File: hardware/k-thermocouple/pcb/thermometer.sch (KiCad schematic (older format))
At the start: 25 parts

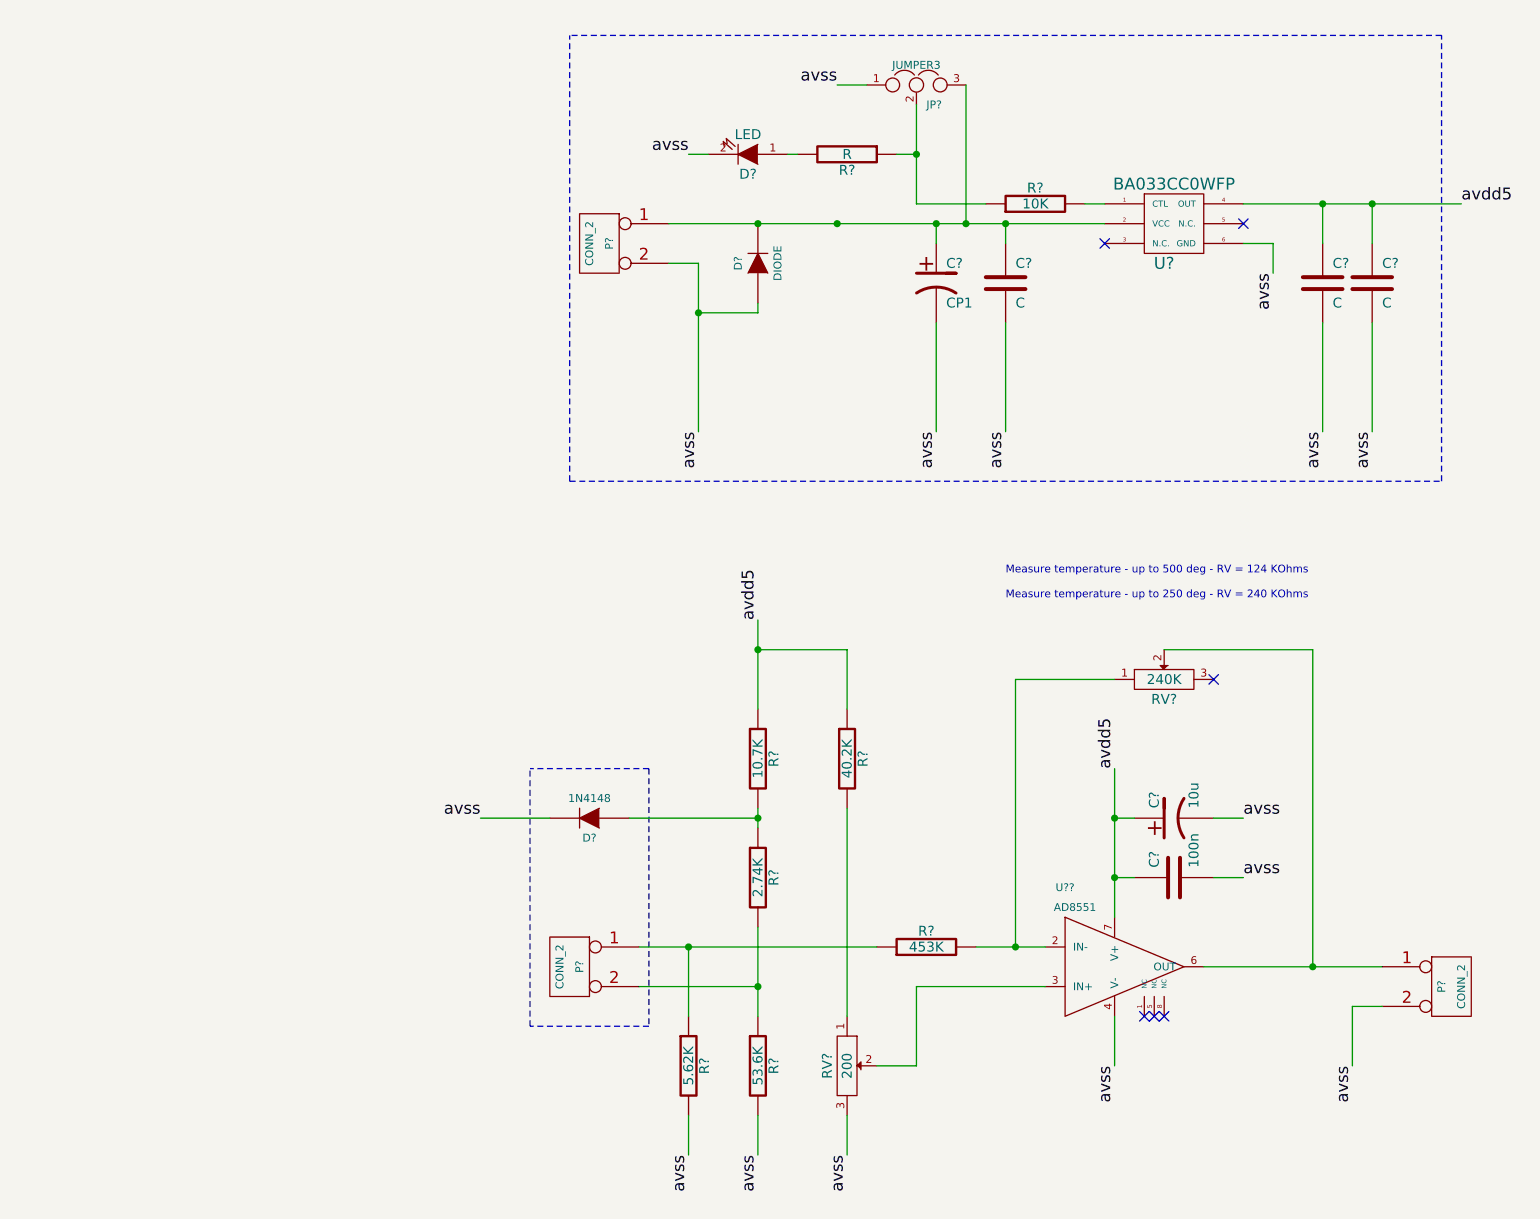
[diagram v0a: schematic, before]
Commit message: Schematic with AD8551 done and initial board started.
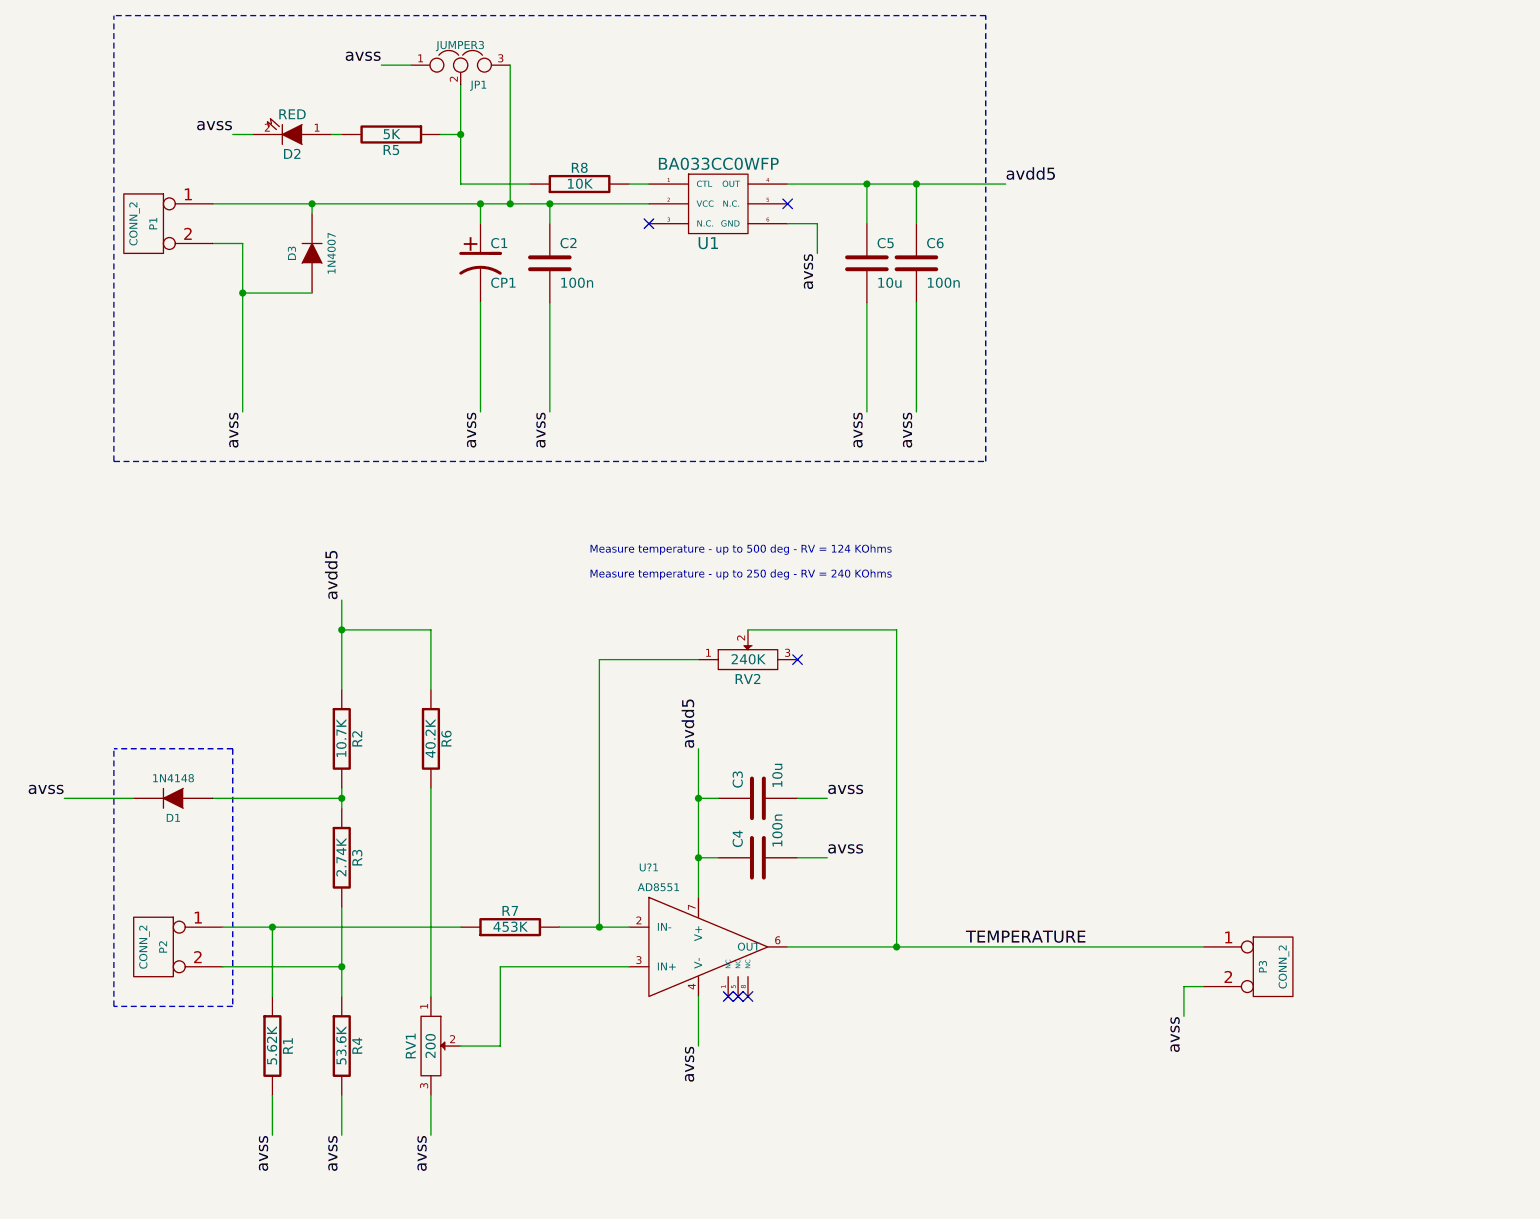
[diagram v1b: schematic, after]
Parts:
- removed C?: 10u, symbol CP1
- removed P?: CONN_2, symbol CONN_2
- added C3: 10u, SM0805, symbol C
- added P3: CONN_2, TS-501, symbol CONN_2
- C1: renamed from C?; footprint (none) -> CAP_POL_10u
- C2, C6: renamed from C?; value C -> 100n; footprint (none) -> SM0805
- C4: renamed from C?; footprint (none) -> SM0805
- C5: renamed from C?; value C -> 10u; footprint (none) -> SM0805
- D1: renamed from D?; footprint (none) -> melf
- D2: renamed from D?; value LED -> RED; footprint (none) -> KP-2012ZGC
- D3: renamed from D?; value DIODE -> 1N4007; footprint (none) -> melf
- JP1: renamed from JP?; footprint (none) -> JUMPER3
- P1: renamed from P?; footprint (none) -> TS-501
- P2: renamed from P?; footprint (none) -> 2EDGR
- R1, R2, R3, R4, R6, R7, R8: renamed from R?; footprint (none) -> SM0805
- R5: renamed from R?; value R -> 5K; footprint (none) -> SM0805
- RV1, RV2: renamed from RV?; footprint (none) -> BOURNS_TRIMMER
- U1: renamed from U?; footprint (none) -> BA033CCOWFP
- U?1: renamed from U??; footprint (none) -> MSOP_8
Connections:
- net avdd5: now also C3.1
- net avss: now also C3.2, P3.2 (PM)
- net TEMPERATURE: now reaches RV2.2, U?1.6 (OUT)
- net TEMPERATURE: now also P3.1 (P1)
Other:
- moved on the sheet: C1, C2, C4, C5, C6, D1, D2, D3, JP1, P1, P2, R1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

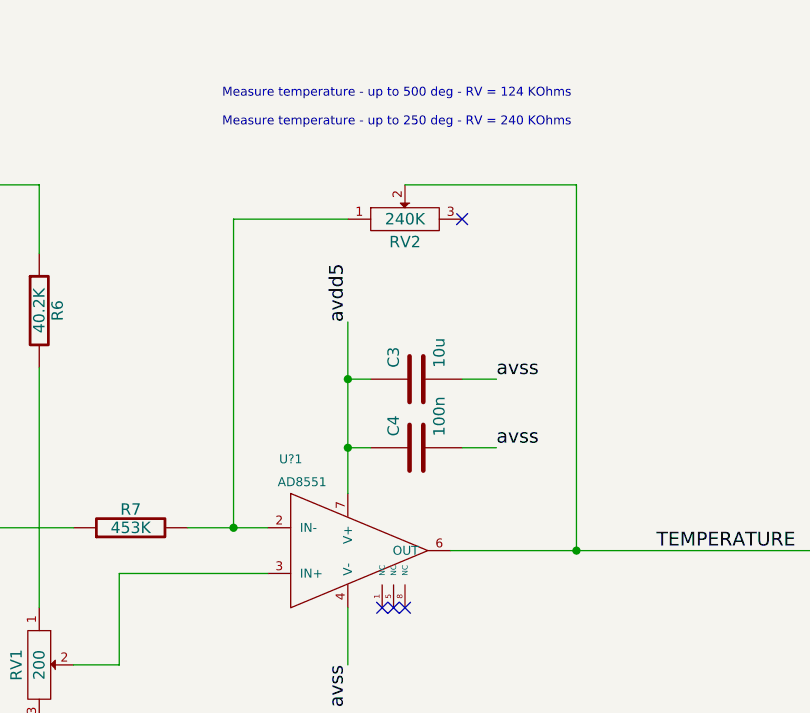
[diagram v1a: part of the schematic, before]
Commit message: Board started and pwr routed.
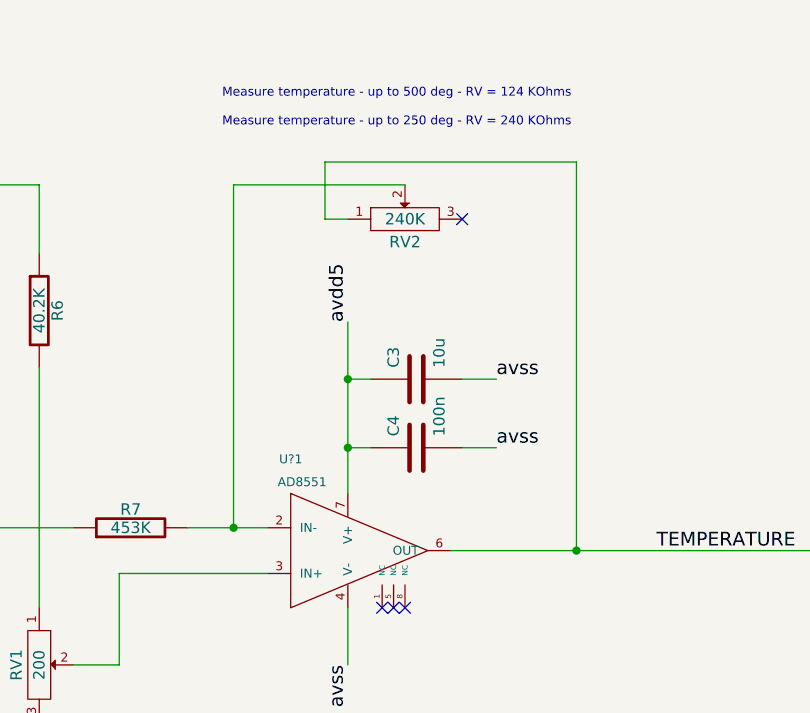
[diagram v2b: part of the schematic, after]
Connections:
- net TEMPERATURE: now also RV2.1; no longer RV2.2
- net at R7.2, U?1.2 (IN-): now also RV2.2; no longer RV2.1
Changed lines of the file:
@@
-EESchema Schematic File Version 2  date Fri 29 Jun 2012 06:34:02 PM EEST
+EESchema Schematic File Version 2  date Fri 06 Jul 2012 05:40:57 PM EEST
 LIBS:power
 LIBS:device
@@
 Sheet 1 1
 Title ""
-Date "29 jun 2012"
+Date "6 jul 2012"
 Rev ""
 Comp ""
@@
 Comment4 ""
 $EndDescr
-Text Label 6850 5950 3    60   ~ 0
-avss
+Wire Wire Line
+	3900 4000 4650 4000
+Wire Wire Line
+	3900 5500 3900 4000
 Wire Wire Line
 	6850 5950 6850 5800
@@
 Wire Wire Line
 	2150 1500 2050 1500
-Wire Wire Line
-	5400 5600 5400 4000
-Wire Wire Line
-	5400 4000 4650 4000
 Wire Wire Line
 	4900 4850 5050 4850
@@
 	4500 4850 4400 4850
 Connection ~ 4400 4850
-Wire Wire Line
-	3900 5500 3900 4150
-Wire Wire Line
-	3900 4150 4400 4150
 Connection ~ 3900 5500
 Connection ~ 5400 5600
@@
 Wire Wire Line
 	6950 5600 4850 5600
+Wire Wire Line
+	5400 5600 5400 3900
+Wire Wire Line
+	5400 3900 4300 3900
+Wire Wire Line
+	4300 3900 4300 4150
+Wire Wire Line
+	4300 4150 4400 4150
+Text Label 6850 5950 3    60   ~ 0
+avss
 $Comp
 L CONN_2 P3
